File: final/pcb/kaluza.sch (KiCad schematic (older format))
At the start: 141 parts

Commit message: new layout
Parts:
- removed D? (x2): SMD_123, Keebio Parts:Diode-Hybrid-Back, symbol Device:D
- removed MX? (x2): MX-NoLED-MX_Alps_Hybrid, Keebio Parts:MX-Alps-Choc-1U, symbol KeyboardMasterList:MX-NoLED-MX_Alps_Hybrid
- added D?: SMD_123, Keebio Parts:Diode-Hybrid-Back, symbol Device:D
- added MX?: MX-NoLED-MX_Alps_Hybrid, Keebio Parts:MX-Alps-Choc-1U, symbol KeyboardMasterList:MX-NoLED-MX_Alps_Hybrid
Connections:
- net COL_0: now also MX?.1 (COL), MX?.1 (COL), MX?.1 (COL), MX?.1 (COL), MX?.1 (COL)
- net COL_1: now also MX?.1 (COL), MX?.1 (COL), MX?.1 (COL), MX?.1 (COL), MX?.1 (COL)
- net COL_10: now also MX?.1 (COL), MX?.1 (COL), MX?.1 (COL), MX?.1 (COL), MX?.1 (COL)
- net COL_11: now also MX?.1 (COL), MX?.1 (COL), MX?.1 (COL), MX?.1 (COL), MX?.1 (COL)
- net COL_12: now also MX?.1 (COL), MX?.1 (COL), MX?.1 (COL), MX?.1 (COL), MX?.1 (COL)
- net COL_13: now also MX?.1 (COL), MX?.1 (COL), MX?.1 (COL), MX?.1 (COL)
- net COL_14: now also MX?.1 (COL), MX?.1 (COL), MX?.1 (COL), SW?.S2, MX?.1 (COL)
- net COL_2: now also MX?.1 (COL), MX?.1 (COL), MX?.1 (COL), MX?.1 (COL), MX?.1 (COL)
- net COL_3: now also MX?.1 (COL), MX?.1 (COL), MX?.1 (COL), MX?.1 (COL)
- net COL_4: now also MX?.1 (COL), MX?.1 (COL), MX?.1 (COL), MX?.1 (COL)
- net COL_5: now also MX?.1 (COL), MX?.1 (COL), MX?.1 (COL), MX?.1 (COL)
- net COL_6: now also MX?.1 (COL), MX?.1 (COL), MX?.1 (COL), MX?.1 (COL), MX?.1 (COL)
- net COL_7: now also MX?.1 (COL), MX?.1 (COL), MX?.1 (COL), MX?.1 (COL)
- net COL_8: now also MX?.1 (COL), MX?.1 (COL), MX?.1 (COL), MX?.1 (COL)
- net COL_9: now also MX?.1 (COL), MX?.1 (COL), MX?.1 (COL), MX?.1 (COL), MX?.1 (COL)
- net ROW0: now also D?.1 (K), D?.1 (K), D?.1 (K), D?.1 (K), D?.1 (K), D?.1 (K), D?.1 (K), D?.1 (K), D?.1 (K), D?.1 (K), D?.1 (K), D?.1 (K), D?.1 (K), D?.1 (K), D?.1 (K)
- net ROW1: now also D?.1 (K), D?.1 (K), D?.1 (K), D?.1 (K), D?.1 (K), D?.1 (K), D?.1 (K), D?.1 (K), D?.1 (K), D?.1 (K), D?.1 (K), D?.1 (K), D?.1 (K), D?.1 (K), D?.1 (K)
- net ROW2: now also D?.1 (K), D?.1 (K), D?.1 (K), D?.1 (K), D?.1 (K), D?.1 (K), D?.1 (K), D?.1 (K), D?.1 (K), D?.1 (K), D?.1 (K), D?.1 (K), D?.1 (K), D?.1 (K)
- net ROW3: now also D?.1 (K), D?.1 (K), D?.1 (K), D?.1 (K), D?.1 (K), D?.1 (K), D?.1 (K), D?.1 (K), D?.1 (K), D?.1 (K), D?.1 (K), D?.1 (K), D?.1 (K), D?.1 (K), SW?.S1
- net ROW4: now also D?.1 (K), D?.1 (K), D?.1 (K), D?.1 (K), D?.1 (K), D?.1 (K), D?.1 (K), D?.1 (K), D?.1 (K), D?.1 (K)
- new net: D?.2 (A), MX?.2 (ROW)
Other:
- note added: "'"
- note added: ","
- note added: "-"
- note added: "."
- note added: "/"
- note added: "0"
- note added: "1"
- note added: "2"
- note added: "3"
- note added: "4"
- note added: "5"
- note added: "6"
- note added: "7"
- note added: "8"
- note added: "9"
- note added: ";"
- note added: "="
- note added: "A"
- note added: "Alt"
- note added: "B"
- note added: "C"
- note added: "Caps"
- note added: "Ctrl"
- note added: "D"
- note added: "Del"
- note added: "Down"
- note added: "E"
- note added: "Enter"
- note added: "Esc"
- note added: "F"
- note added: "F13"
- note added: "F14"
- note added: "F15"
- note added: "Fn"
- note added: "G"
- note added: "H"
- note added: "I"
- note added: "J"
- note added: "K"
- note added: "L"
- note added: "Left"
- note added: "M"
- note added: "Mute"
- note added: "N"
- note added: "O"
- note added: "P"
- note added: "Q"
- note added: "R"
- note added: "RCtrl"
- note added: "RShift\n"
- note added: "Right"
- note added: "S"
- note added: "Shift"
- note added: "Space"
- note added: "T"
- note added: "Tab"
- note added: "U"
- note added: "Up"
- note added: "V"
- note added: "W"
- note added: "Win"
- note added: "X"
- note added: "Y"
- note added: "Z"
- note added: "["
- note added: "\"
- note added: "]"
- moved on the sheet: D?, MX?, OL?, SW?, U?

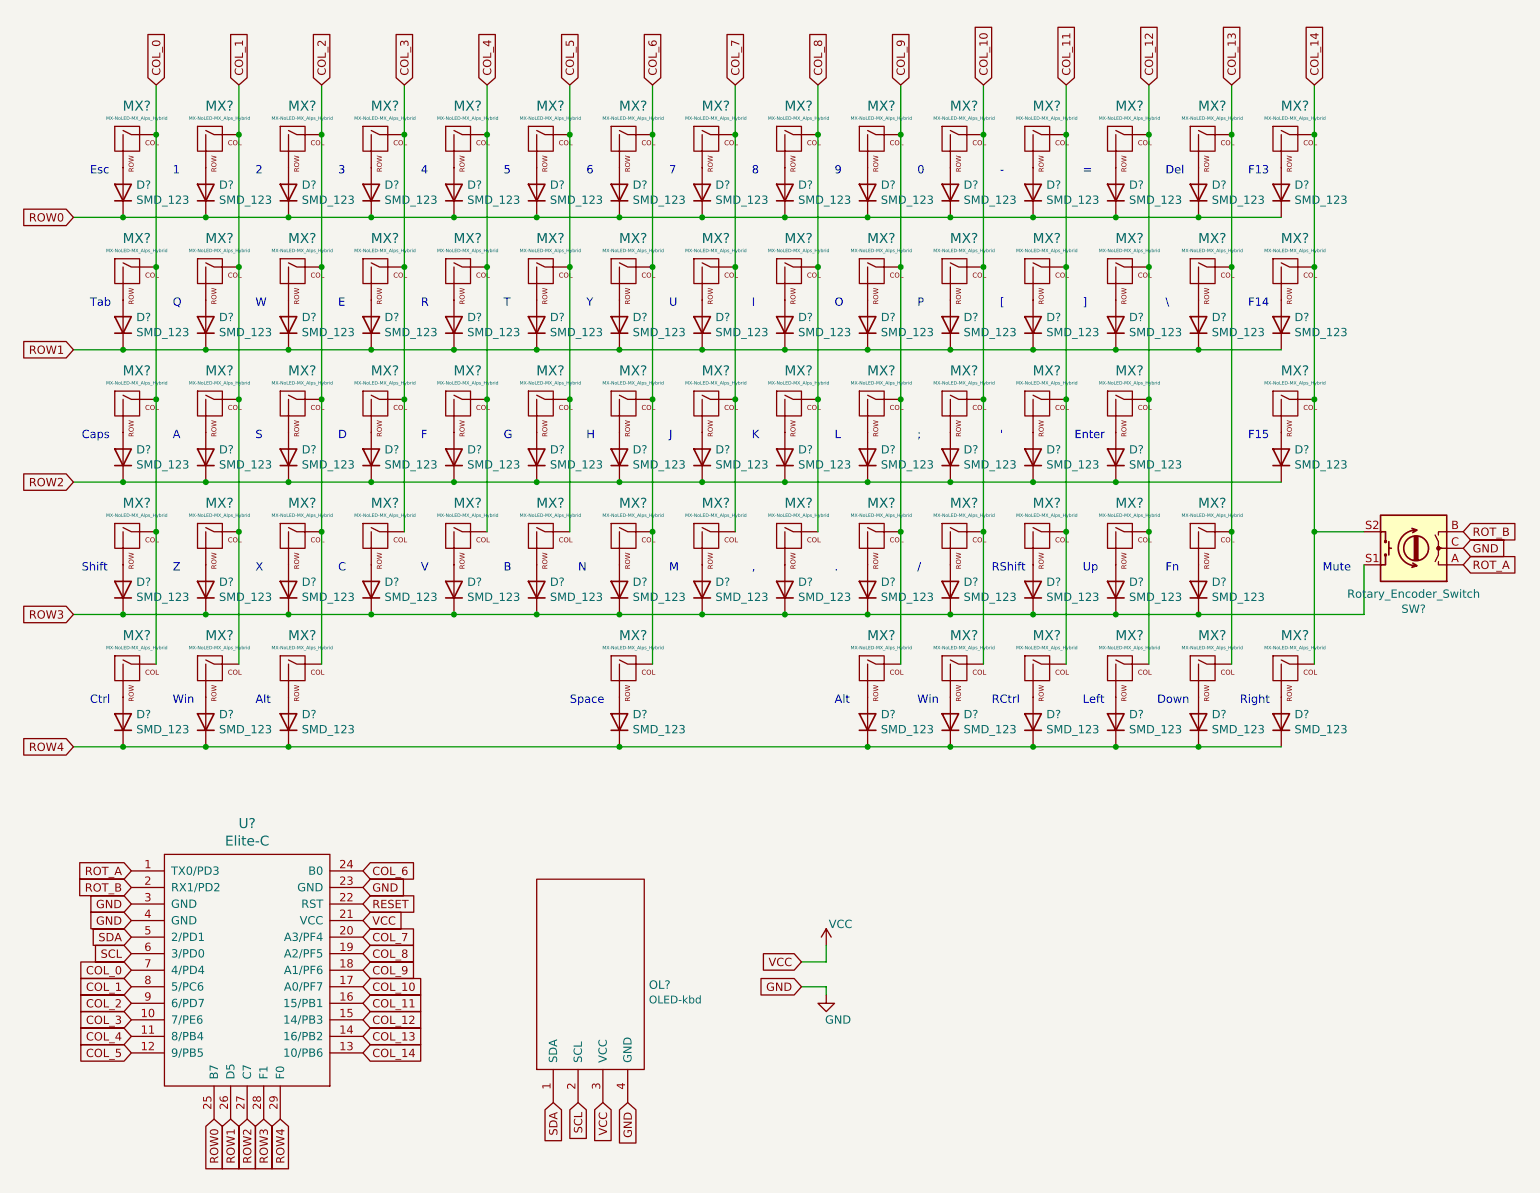
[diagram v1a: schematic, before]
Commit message: laid out basically everything but diodes on pcb
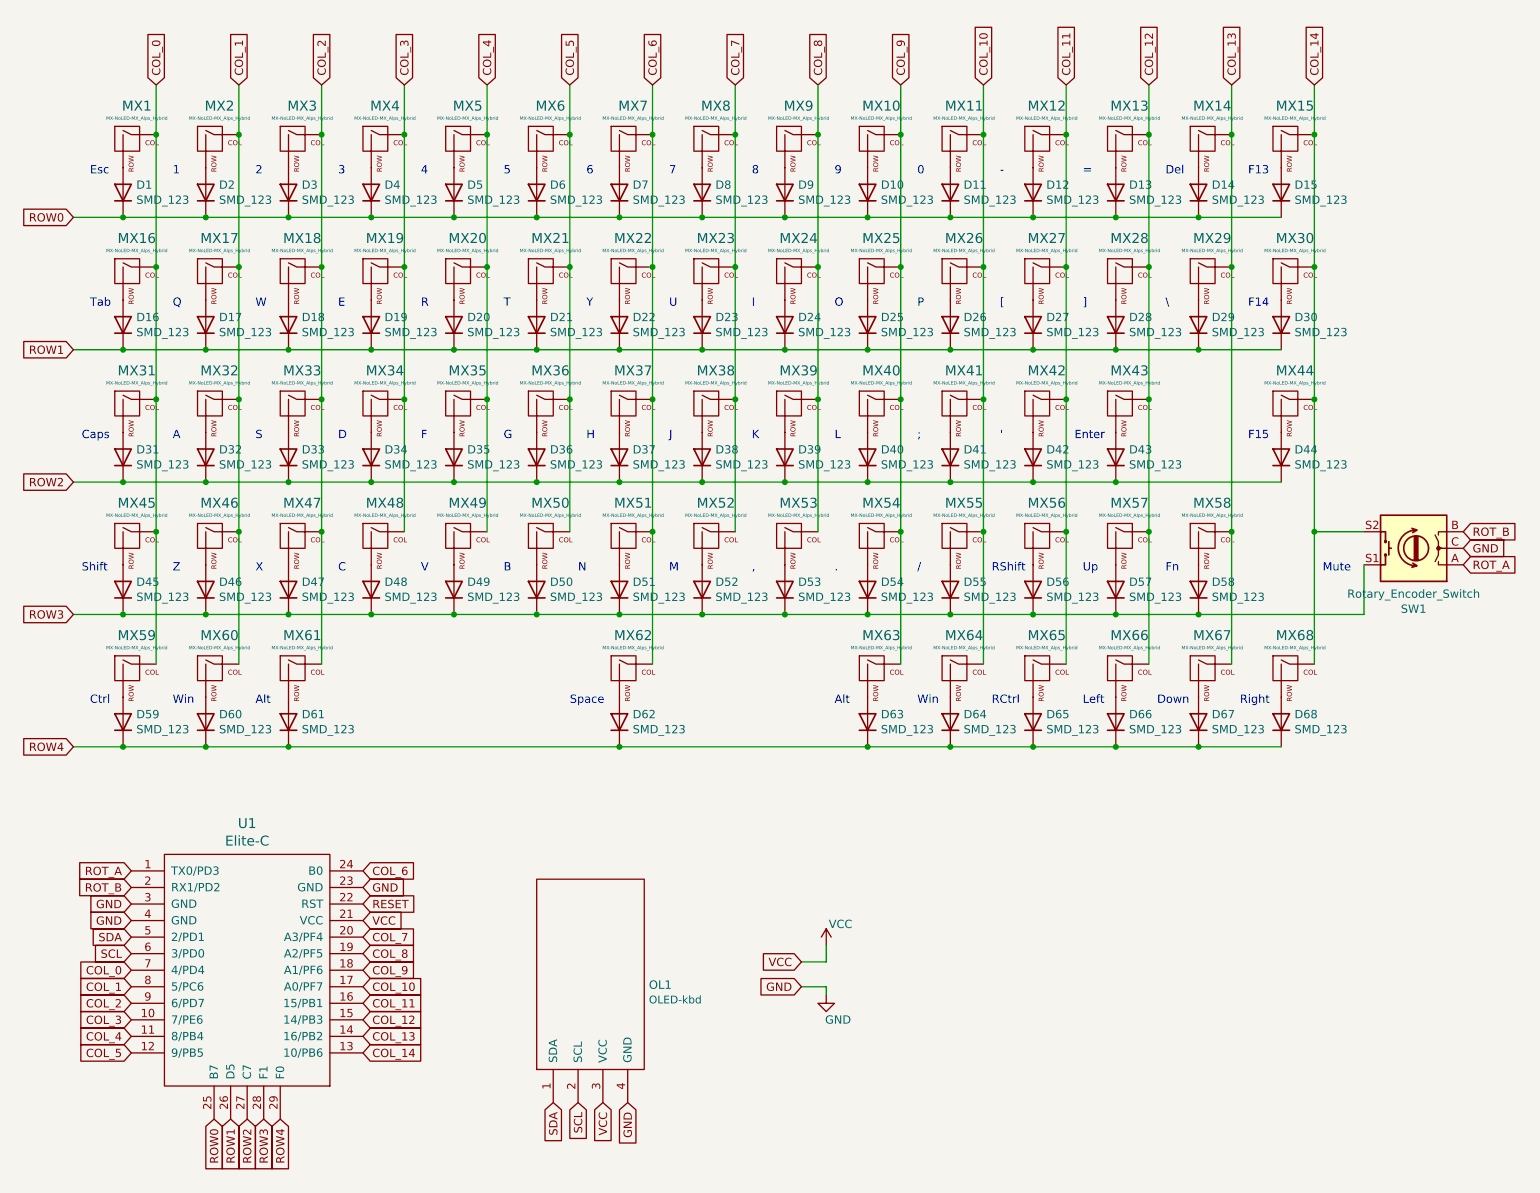
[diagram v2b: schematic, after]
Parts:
- gave numbers to parts that had none: 139

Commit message: update
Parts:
- MX1, MX10, MX11, MX12, MX13, MX15, MX17, MX18, MX19, MX2, MX20, MX21, MX22, MX23, MX24, MX25, MX26, MX27, MX28, MX3, MX30, MX32, MX33, MX34, MX35, MX36, MX37, MX38, MX39, MX4, MX40, MX41, MX42, MX44, MX46, MX47, MX48, MX49, MX5, MX50, MX51, MX52, MX53, MX54, MX55, MX57, MX58, MX6, MX63, MX64, MX65, MX66, MX67, MX68, MX7, MX8, MX9: footprint Keebio Parts:MX-Alps-Choc-1U -> Keyboard Master List:MX-1U
- MX14: footprint Keebio Parts:MX-Alps-Choc-1U -> Keyboard Master List:MX-2U
- MX16, MX29: footprint Keebio Parts:MX-Alps-Choc-1U -> Keyboard Master List:MX-1.5U
- MX31, MX56: footprint Keebio Parts:MX-Alps-Choc-1U -> Keyboard Master List:MX-1.75U
- MX43, MX45: footprint Keebio Parts:MX-Alps-Choc-1U -> Keyboard Master List:MX-2.25U
- MX59, MX60, MX61: footprint Keebio Parts:MX-Alps-Choc-1U -> Keyboard Master List:MX-1.25U
- MX62: footprint Keebio Parts:MX-Alps-Choc-1U -> Keyboard Master List:MX-6.25U
